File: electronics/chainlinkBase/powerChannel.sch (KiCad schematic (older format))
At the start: 14 parts, among them J201 CHANNEL, U201 INA219BxD, U202 VN7007ALH

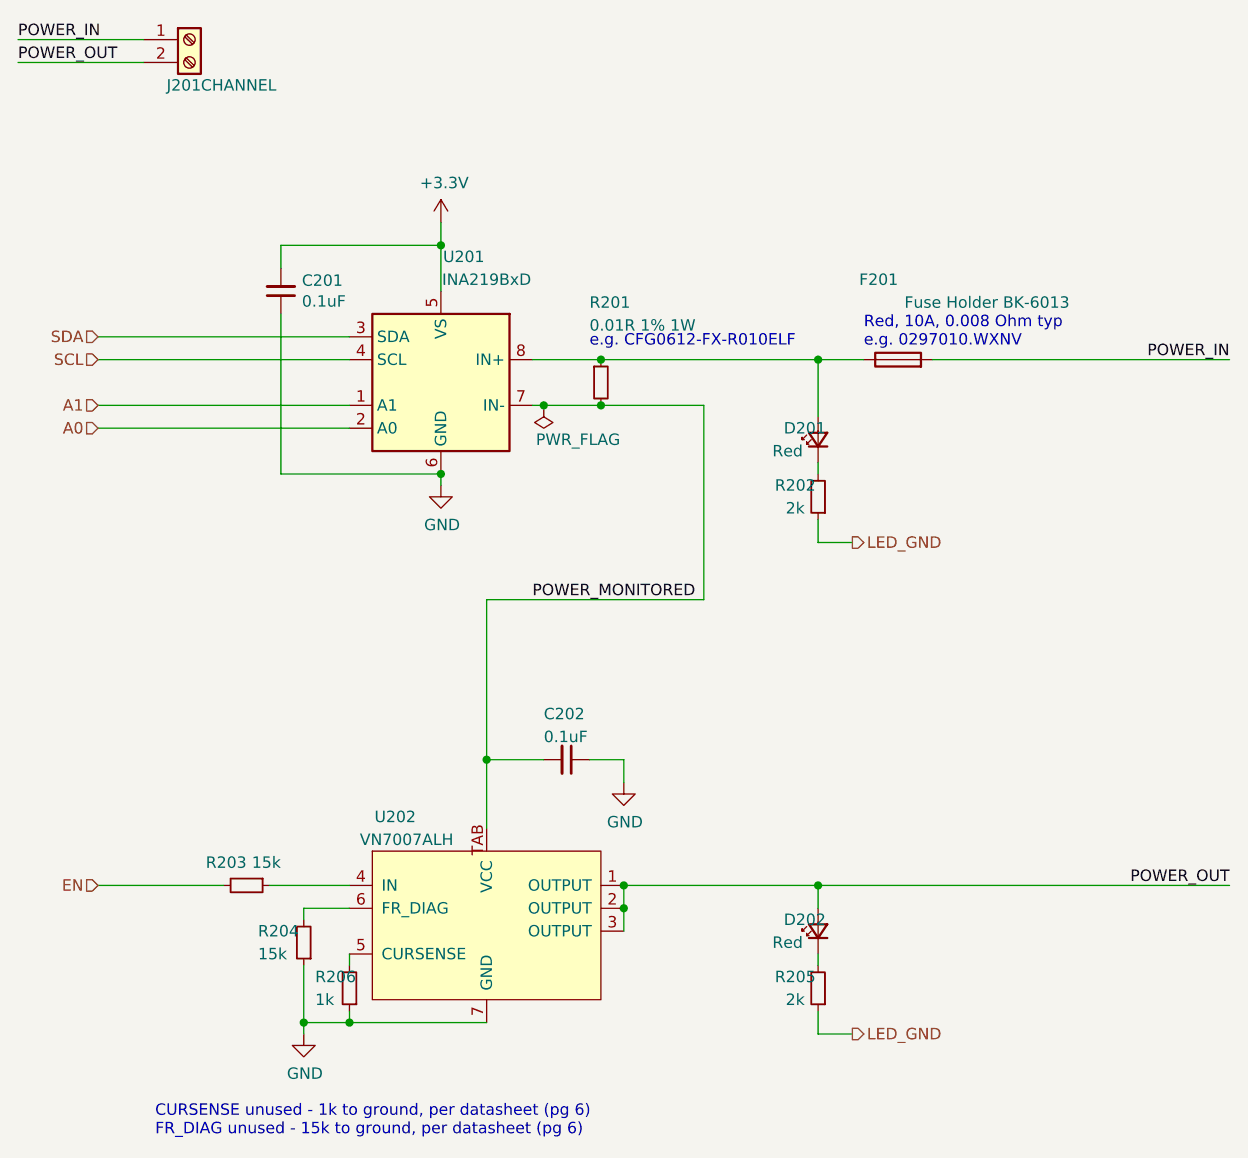
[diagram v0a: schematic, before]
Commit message: Chainlink Base - Digikey part numbers, schematic cleanup, minor pcb tweaks
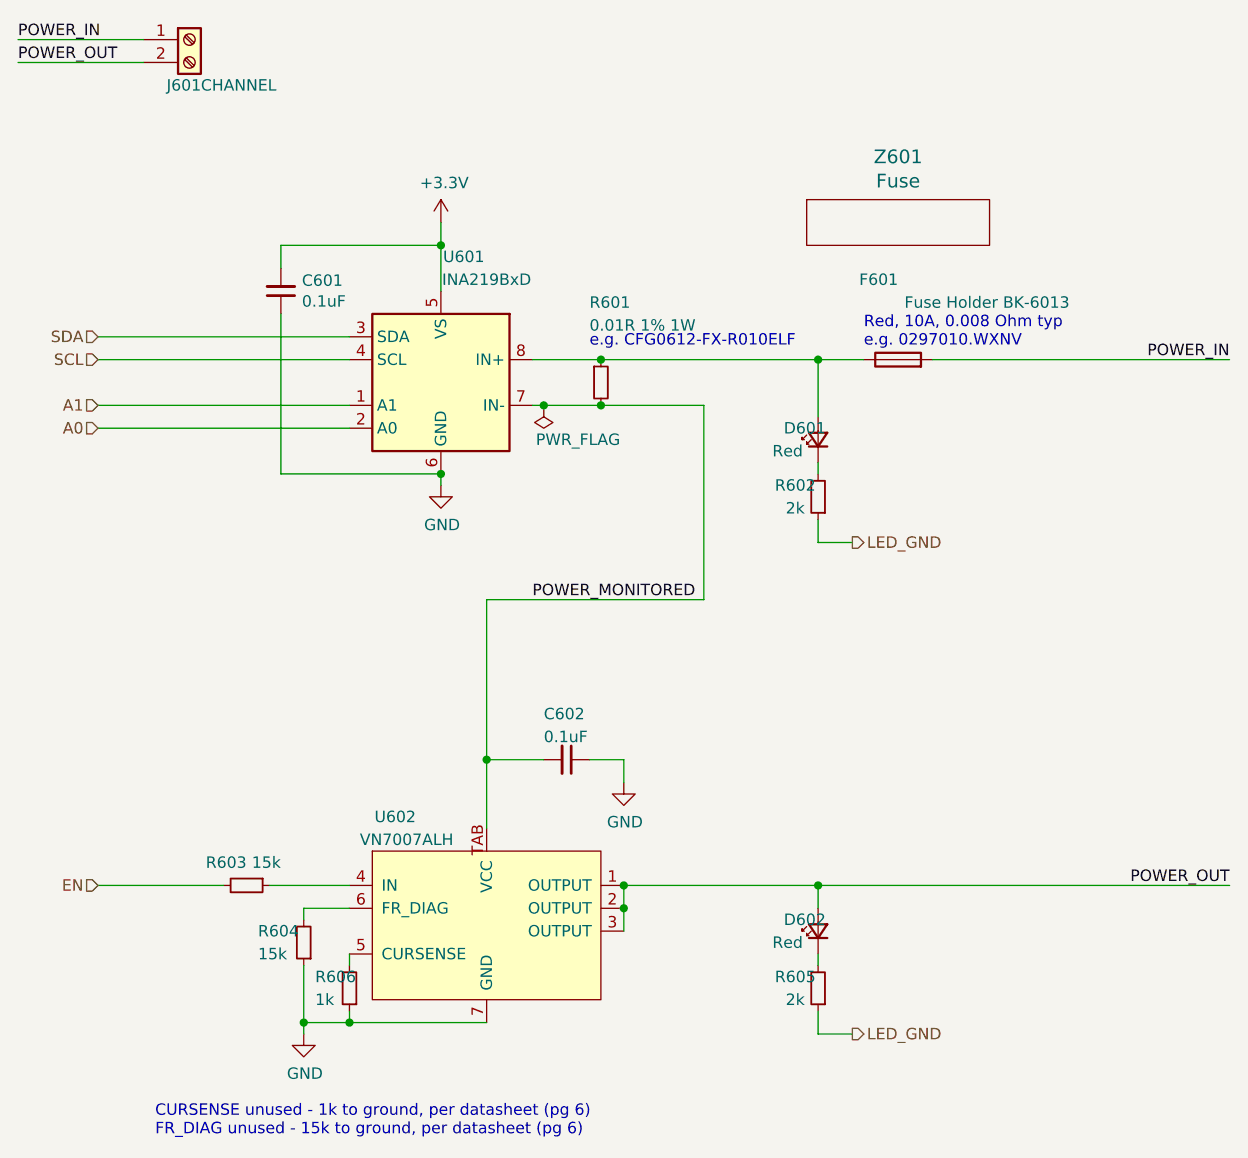
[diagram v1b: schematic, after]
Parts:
- added Z201: Fuse, Dummy:Dummy, symbol no_pin:no_pin
- C201, C202: DK# (none) -> 1276-2449-1-ND
- D201, D202: DK# (none) -> 475-1278-1-ND
- R202, R205: DK# (none) -> RMCF0805JT2K00CT-ND
- R203, R204: DK# (none) -> RMCF0805JT15K0CT-ND
- R206: DK# (none) -> RMCF0805JT1K00CT-ND
- U202: DK# (none) -> 497-16868-1-ND
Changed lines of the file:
@@
 $Descr A4 11693 8268
 encoding utf-8
-Sheet 2 6
+Sheet 6 6
 Title ""
 Date ""
@@
 AR Path="/60B0E338/60718742" Ref="C501"  Part="1"
 AR Path="/60B1F5E9/60718742" Ref="C601"  Part="1"
-F 0 "C201" H 2208 1804 50  0000 R CNN
+F 0 "C601" H 2208 1804 50  0000 R CNN
 F 1 "0.1uF" H 2208 1895 50  0000 R CNN
 F 2 "Capacitor_SMD:C_0805_2012Metric" H 2300 1850 50  0001 C CNN
 F 3 "~" H 2300 1850 50  0001 C CNN
+F 4 "1276-2449-1-ND" H 2300 1850 50  0001 C CNN "DK#"
 	1    2300 1850
 	-1   0    0    1
@@
 AR Path="/60B0E338/6071874C" Ref="D502"  Part="1"
 AR Path="/60B1F5E9/6071874C" Ref="D602"  Part="1"
-F 0 "D202" V 4700 4800 50  0000 R CNN
+F 0 "D602" V 4700 4800 50  0000 R CNN
 F 1 "Red" V 4600 4850 50  0000 R CNN
 F 2 "LED_SMD:LED_0805_2012Metric" V 4650 4650 50  0001 C CNN
 F 3 "~" V 4650 4650 50  0001 C CNN
+F 4 "475-1278-1-ND" H 4650 4650 50  0001 C CNN "DK#"
 	1    4650 4650
 	0    -1   -1   0
@@
 AR Path="/60B0E338/60718752" Ref="#PWR0505"  Part="1"
 AR Path="/60B1F5E9/60718752" Ref="#PWR0605"  Part="1"
-F 0 "#PWR0205" H 2400 4850 50  0001 C CNN
+F 0 "#PWR0605" H 2400 4850 50  0001 C CNN
 F 1 "GND" H 2405 4927 50  0000 C CNN
 F 2 "" H 2400 5100 50  0001 C CNN
@@
 AR Path="/60B0E338/60718758" Ref="R505"  Part="1"
 AR Path="/60B1F5E9/60718758" Ref="R605"  Part="1"
-F 0 "R205" H 4750 4850 50  0000 C CNN
+F 0 "R605" H 4750 4850 50  0000 C CNN
 F 1 "2k" H 4750 4950 50  0000 C CNN
 F 2 "Resistor_SMD:R_0805_2012Metric" H 4650 4900 50  0001 C CNN
 F 3 "~" H 4650 4900 50  0001 C CNN
+F 4 "RMCF0805JT2K00CT-ND" H 4650 4900 50  0001 C CNN "DK#"
 	1    4650 4900
 	-1   0    0    1
@@
 AR Path="/60B0E338/6071875F" Ref="C502"  Part="1"
 AR Path="/60B1F5E9/6071875F" Ref="C602"  Part="1"
-F 0 "C202" V 3350 3800 50  0000 L CNN
+F 0 "C602" V 3350 3800 50  0000 L CNN
 F 1 "0.1uF" V 3450 3800 50  0000 L CNN
 F 2 "Capacitor_SMD:C_0805_2012Metric" H 3550 3900 50  0001 C CNN
 F 3 "~" H 3550 3900 50  0001 C CNN
+F 4 "1276-2449-1-ND" H 3550 3900 50  0001 C CNN "DK#"
 	1    3550 3900
 	0    1    1    0
@@
 AR Path="/60B0E338/6071876B" Ref="#PWR0501"  Part="1"
 AR Path="/60B1F5E9/6071876B" Ref="#PWR0601"  Part="1"
-F 0 "#PWR0201" H 3000 1400 50  0001 C CNN
+F 0 "#PWR0601" H 3000 1400 50  0001 C CNN
 F 1 "+3.3V" H 3015 1723 50  0000 C CNN
 F 2 "" H 3000 1550 50  0001 C CNN
@@
 AR Path="/60B0E338/60718772" Ref="#PWR0502"  Part="1"
 AR Path="/60B1F5E9/60718772" Ref="#PWR0602"  Part="1"
-F 0 "#PWR0202" H 3000 2450 50  0001 C CNN
+F 0 "#PWR0602" H 3000 2450 50  0001 C CNN
 F 1 "GND" H 3005 2527 50  0000 C CNN
 F 2 "" H 3000 2700 50  0001 C CNN
@@
 AR Path="/60B0E338/6071877C" Ref="R501"  Part="1"
 AR Path="/60B1F5E9/6071877C" Ref="R601"  Part="1"
-F 0 "R201" H 3650 2600 50  0000 L CNN
+F 0 "R601" H 3650 2600 50  0000 L CNN
 F 1 "0.01R 1% 1W" H 3650 2500 50  0000 L CNN
 F 2 "Resistor_SMD:R_0612_1632Metric" H 3700 2250 50  0001 C CNN
@@
 AR Path="/60B0E338/60718784" Ref="F501"  Part="1"
 AR Path="/60B1F5E9/60718784" Ref="F601"  Part="1"
-F 0 "F201" V 5350 2150 50  0000 L CNN
+F 0 "F601" V 5350 2150 50  0000 L CNN
 F 1 "Fuse Holder BK-6013" V 5250 1400 50  0000 L CNN
 F 2 "BK-6013:BK-6013" V 4930 2150 50  0001 C CNN
@@
 AR Path="/60B0E338/6071879D" Ref="R503"  Part="1"
 AR Path="/60B1F5E9/6071879D" Ref="R603"  Part="1"
-F 0 "R203" V 2050 4450 50  0000 R CNN
+F 0 "R603" V 2050 4450 50  0000 R CNN
 F 1 "15k" V 2050 4600 50  0000 R CNN
 F 2 "Resistor_SMD:R_0805_2012Metric" H 2150 4450 50  0001 C CNN
 F 3 "~" H 2150 4450 50  0001 C CNN
+F 4 "RMCF0805JT15K0CT-ND" H 2150 4450 50  0001 C CNN "DK#"
 	1    2150 4450
 	0    1    1    0
@@
 AR Path="/60B0E338/607187A4" Ref="J501"  Part="1"
 AR Path="/60B1F5E9/607187A4" Ref="J601"  Part="1"
-F 0 "J201" H 1800 550 50  0000 L CNN
+F 0 "J601" H 1800 550 50  0000 L CNN
 F 1 "CHANNEL" H 1950 550 50  0000 L CNN
 F 2 "ScrewTerminals:Generic-5.08-2P" H 1900 750 50  0001 C CNN
@@
 AR Path="/60B0E338/607187AC" Ref="#FLG0501"  Part="1"
 AR Path="/60B1F5E9/607187AC" Ref="#FLG0601"  Part="1"
-F 0 "#FLG0201" H 3450 2425 50  0001 C CNN
+F 0 "#FLG0601" H 3450 2425 50  0001 C CNN
 F 1 "PWR_FLAG" H 3300 2500 50  0000 C CNN
 F 2 "" H 3450 2350 50  0001 C CNN
@@
 AR Path="/60B0E338/607187B2" Ref="U502"  Part="1"
 AR Path="/60B1F5E9/607187B2" Ref="U602"  Part="1"
-F 0 "U202" H 2800 4950 50  0000 C CNN
+F 0 "U602" H 2800 4950 50  0000 C CNN
 F 1 "VN7007ALH" H 2850 4850 50  0000 C CNN
 F 2 "VN7007ALHTR:VN7007ALHTR" H 3200 4550 50  0001 C CNN
 F 3 "" H 3200 4550 50  0001 C CNN
+F 4 "497-16868-1-ND" H 3200 4550 50  0001 C CNN "DK#"
 	1    3200 4550
 	1    0    0    -1
@@
 AR Path="/60B0E338/607187BF" Ref="R506"  Part="1"
 AR Path="/60B1F5E9/607187BF" Ref="R606"  Part="1"
-F 0 "R206" H 2750 4850 50  0000 R CNN
+F 0 "R606" H 2750 4850 50  0000 R CNN
 F 1 "1k" H 2750 4950 50  0000 R CNN
 F 2 "Resistor_SMD:R_0805_2012Metric" H 2600 4900 50  0001 C CNN
 F 3 "~" H 2600 4900 50  0001 C CNN
+F 4 "RMCF0805JT1K00CT-ND" H 2600 4900 50  0001 C CNN "DK#"
 	1    2600 4900
 	-1   0    0    1
@@
 AR Path="/60B0E338/607187C9" Ref="R504"  Part="1"
 AR Path="/60B1F5E9/607187C9" Ref="R604"  Part="1"
-F 0 "R204" H 2600 4650 50  0000 R CNN
+F 0 "R604" H 2600 4650 50  0000 R CNN
 F 1 "15k" H 2600 4750 50  0000 R CNN
 F 2 "Resistor_SMD:R_0805_2012Metric" H 2400 4700 50  0001 C CNN
 F 3 "~" H 2400 4700 50  0001 C CNN
+F 4 "RMCF0805JT15K0CT-ND" H 2400 4700 50  0001 C CNN "DK#"
 	1    2400 4700
 	-1   0    0    1
@@
 AR Path="/60B0E338/607187E7" Ref="D501"  Part="1"
 AR Path="/60B1F5E9/607187E7" Ref="D601"  Part="1"
-F 0 "D201" V 4700 2650 50  0000 R CNN
+F 0 "D601" V 4700 2650 50  0000 R CNN
 F 1 "Red" V 4600 2700 50  0000 R CNN
 F 2 "LED_SMD:LED_0805_2012Metric" V 4650 2500 50  0001 C CNN
 F 3 "~" V 4650 2500 50  0001 C CNN
+F 4 "475-1278-1-ND" H 4650 2500 50  0001 C CNN "DK#"
 	1    4650 2500
 	0    -1   -1   0
@@
 AR Path="/60B0E338/607187ED" Ref="R502"  Part="1"
 AR Path="/60B1F5E9/607187ED" Ref="R602"  Part="1"
-F 0 "R202" H 4750 2700 50  0000 C CNN
+F 0 "R602" H 4750 2700 50  0000 C CNN
 F 1 "2k" H 4750 2800 50  0000 C CNN
 F 2 "Resistor_SMD:R_0805_2012Metric" H 4650 2750 50  0001 C CNN
 F 3 "~" H 4650 2750 50  0001 C CNN
+F 4 "RMCF0805JT2K00CT-ND" H 4650 2750 50  0001 C CNN "DK#"
 	1    4650 2750
 	-1   0    0    1
@@
 AR Path="/60B0E338/6071873C" Ref="U501"  Part="1"
 AR Path="/60B1F5E9/6071873C" Ref="U601"  Part="1"
-F 0 "U201" H 2900 2800 50  0000 C CNN
+F 0 "U601" H 2900 2800 50  0000 C CNN
 F 1 "INA219BxD" H 2800 2700 50  0000 C CNN
 F 2 "Package_SO:SOIC-8_3.9x4.9mm_P1.27mm" H 3800 1900 50  0001 C CNN
@@
 AR Path="/60B0E338/60762DAE" Ref="#PWR0504"  Part="1"
 AR Path="/60B1F5E9/60762DAE" Ref="#PWR0604"  Part="1"
-F 0 "#PWR0204" H 3800 3750 50  0001 C CNN
+F 0 "#PWR0604" H 3800 3750 50  0001 C CNN
 F 1 "GND" H 3805 3827 50  0000 C CNN
 F 2 "" H 3800 4000 50  0001 C CNN
@@
 Wire Wire Line
 	4650 4450 6450 4450
+$Comp
+L no_pin:no_pin Z201
+U 1 1 6078F8EB
+P 5000 1550
+AR Path="/606FA86C/6078F8EB" Ref="Z201"  Part="1"
+AR Path="/60AEE6BF/6078F8EB" Ref="Z301"  Part="1"
+AR Path="/60AFE278/6078F8EB" Ref="Z401"  Part="1"
+AR Path="/60B0E338/6078F8EB" Ref="Z501"  Part="1"
+AR Path="/60B1F5E9/6078F8EB" Ref="Z601"  Part="1"
+F 0 "Z601" H 5000 1837 60  0000 C CNN
+F 1 "Fuse" H 5000 1731 60  0000 C CNN
+F 2 "Dummy:Dummy" H 5000 1550 60  0001 C CNN
+F 3 "" H 5000 1550 60  0001 C CNN
+F 4 "0297010.WXNV" H 5000 1550 50  0001 C CNN "DK#"
+	1    5000 1550
+	1    0    0    -1
+$EndComp
 $EndSCHEMATC
